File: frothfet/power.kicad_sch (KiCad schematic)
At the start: 46 parts, among them J11 Screw_Terminal_01x08, J12 Screw_Terminal_01x08, U26 TPS7A2033PDBVR, U27 XL1509-5.0, U28 MCP3425A0T-ECH, U29 MAX40200AUK

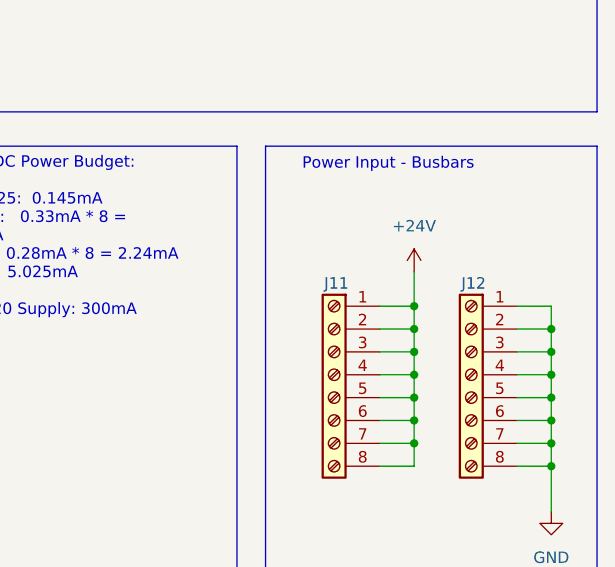
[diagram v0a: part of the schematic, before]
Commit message: rearranged leds and cleaned things up a bit.
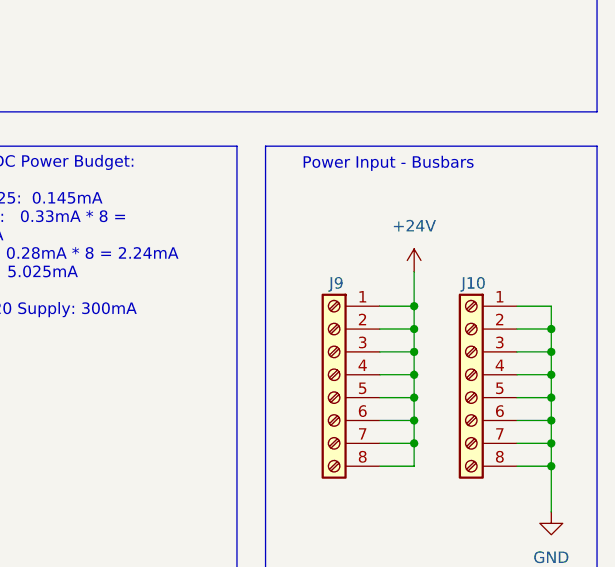
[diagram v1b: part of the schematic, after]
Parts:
- renumbered J12 to J10, J11 to J9
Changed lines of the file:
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@@
 		(on_board yes)
 		(dnp no)
-		(property "Reference" "J11"
+		(property "Reference" "J9"
 			(at 251.714 99.06 0)
 			(effects
@@
 			(project ""
 				(path "/c83c6236-96e9-46ad-9d7a-9e2efa4a7966/e112a34f-fd2f-43cb-bf5d-a7f5e57b6bef"
-					(reference "J11")
+					(reference "J9")
 					(unit 1)
 				)
@@
 		(dnp no)
 		(fields_autoplaced yes)
-		(property "Reference" "#PWR0135"
+		(property "Reference" "#PWR0131"
 			(at 19.05 102.87 0)
 			(effects
@@
 			(project "frothfet"
 				(path "/c83c6236-96e9-46ad-9d7a-9e2efa4a7966/e112a34f-fd2f-43cb-bf5d-a7f5e57b6bef"
-					(reference "#PWR0135")
+					(reference "#PWR0131")
 					(unit 1)
 				)
@@
 		(dnp no)
 		(fields_autoplaced yes)
-		(property "Reference" "#PWR0141"
+		(property "Reference" "#PWR0137"
 			(at 106.68 102.87 0)
 			(effects
@@
 			(project "frothfet"
 				(path "/c83c6236-96e9-46ad-9d7a-9e2efa4a7966/e112a34f-fd2f-43cb-bf5d-a7f5e57b6bef"
-					(reference "#PWR0141")
+					(reference "#PWR0137")
 					(unit 1)
 				)
@@
 		(dnp no)
 		(fields_autoplaced yes)
-		(property "Reference" "#PWR0137"
+		(property "Reference" "#PWR0133"
 			(at 30.48 161.29 0)
 			(effects
@@
 			(project "frothfet"
 				(path "/c83c6236-96e9-46ad-9d7a-9e2efa4a7966/e112a34f-fd2f-43cb-bf5d-a7f5e57b6bef"
-					(reference "#PWR0137")
+					(reference "#PWR0133")
 					(unit 1)
 				)
@@
 		(dnp no)
 		(fields_autoplaced yes)
-		(property "Reference" "#PWR0145"
+		(property "Reference" "#PWR0141"
 			(at 156.21 137.16 0)
 			(effects
@@
 			(project "frothfet"
 				(path "/c83c6236-96e9-46ad-9d7a-9e2efa4a7966/e112a34f-fd2f-43cb-bf5d-a7f5e57b6bef"
-					(reference "#PWR0145")
+					(reference "#PWR0141")
 					(unit 1)
 				)
@@
 		(dnp no)
 		(fields_autoplaced yes)
-		(property "Reference" "#PWR0140"
+		(property "Reference" "#PWR0136"
 			(at 86.36 100.33 0)
 			(effects
@@
 			(project ""
 				(path "/c83c6236-96e9-46ad-9d7a-9e2efa4a7966/e112a34f-fd2f-43cb-bf5d-a7f5e57b6bef"
-					(reference "#PWR0140")
+					(reference "#PWR0136")
 					(unit 1)
 				)
@@
 		(on_board yes)
 		(dnp no)
-		(property "Reference" "J12"
+		(property "Reference" "J10"
 			(at 266.954 99.06 0)
 			(effects
@@
 			(project ""
 				(path "/c83c6236-96e9-46ad-9d7a-9e2efa4a7966/e112a34f-fd2f-43cb-bf5d-a7f5e57b6bef"
-					(reference "J12")
+					(reference "J10")
 					(unit 1)
 				)
@@
 		(dnp no)
 		(fields_autoplaced yes)
-		(property "Reference" "#PWR0138"
+		(property "Reference" "#PWR0134"
 			(at 30.48 187.96 0)
 			(effects
@@
 			(project "frothfet"
 				(path "/c83c6236-96e9-46ad-9d7a-9e2efa4a7966/e112a34f-fd2f-43cb-bf5d-a7f5e57b6bef"
-					(reference "#PWR0138")
+					(reference "#PWR0134")
 					(unit 1)
 				)
@@
 		(dnp no)
 		(fields_autoplaced yes)
-		(property "Reference" "#PWR0142"
+		(property "Reference" "#PWR0138"
 			(at 138.43 107.95 0)
 			(effects
@@
 			(project "8ch-mosfet"
 				(path "/c83c6236-96e9-46ad-9d7a-9e2efa4a7966/e112a34f-fd2f-43cb-bf5d-a7f5e57b6bef"
-					(reference "#PWR0142")
+					(reference "#PWR0138")
 					(unit 1)
 				)
@@
 		(dnp no)
 		(fields_autoplaced yes)
-		(property "Reference" "#PWR0148"
+		(property "Reference" "#PWR0144"
 			(at 275.59 130.81 0)
 			(effects
@@
 			(project "8ch-mosfet"
 				(path "/c83c6236-96e9-46ad-9d7a-9e2efa4a7966/e112a34f-fd2f-43cb-bf5d-a7f5e57b6bef"
-					(reference "#PWR0148")
+					(reference "#PWR0144")
 					(unit 1)
 				)
@@
 		(dnp no)
 		(fields_autoplaced yes)
-		(property "Reference" "#PWR0146"
+		(property "Reference" "#PWR0142"
 			(at 260.35 101.6 0)
 			(effects
@@
 			(project "8ch-mosfet"
 				(path "/c83c6236-96e9-46ad-9d7a-9e2efa4a7966/e112a34f-fd2f-43cb-bf5d-a7f5e57b6bef"
-					(reference "#PWR0146")
+					(reference "#PWR0142")
 					(unit 1)
 				)
@@
 		(dnp no)
 		(fields_autoplaced yes)
-		(property "Reference" "#PWR0143"
+		(property "Reference" "#PWR0139"
 			(at 156.21 64.77 0)
 			(effects
@@
 			(project "8ch-mosfet"
 				(path "/c83c6236-96e9-46ad-9d7a-9e2efa4a7966/e112a34f-fd2f-43cb-bf5d-a7f5e57b6bef"
-					(reference "#PWR0143")
+					(reference "#PWR0139")
 					(unit 1)
 				)
@@
 		(dnp no)
 		(fields_autoplaced yes)
-		(property "Reference" "#PWR0147"
+		(property "Reference" "#PWR0143"
 			(at 266.7 33.02 0)
 			(effects
@@
 			(project "8ch-mosfet"
 				(path "/c83c6236-96e9-46ad-9d7a-9e2efa4a7966/e112a34f-fd2f-43cb-bf5d-a7f5e57b6bef"
-					(reference "#PWR0147")
+					(reference "#PWR0143")
 					(unit 1)
 				)
@@
 		(dnp no)
 		(fields_autoplaced yes)
-		(property "Reference" "#PWR0139"
+		(property "Reference" "#PWR0135"
 			(at 49.53 137.16 0)
 			(effects
@@
 			(project ""
 				(path "/c83c6236-96e9-46ad-9d7a-9e2efa4a7966/e112a34f-fd2f-43cb-bf5d-a7f5e57b6bef"
-					(reference "#PWR0139")
+					(reference "#PWR0135")
 					(unit 1)
 				)
@@
 		(dnp no)
 		(fields_autoplaced yes)
-		(property "Reference" "#PWR0136"
+		(property "Reference" "#PWR0132"
 			(at 22.86 33.02 0)
 			(effects
@@
 			(project "8ch-mosfet"
 				(path "/c83c6236-96e9-46ad-9d7a-9e2efa4a7966/e112a34f-fd2f-43cb-bf5d-a7f5e57b6bef"
-					(reference "#PWR0136")
+					(reference "#PWR0132")
 					(unit 1)
 				)
@@
 		(dnp no)
 		(fields_autoplaced yes)
-		(property "Reference" "#PWR0144"
+		(property "Reference" "#PWR0140"
 			(at 160.02 93.98 0)
 			(effects
@@
 			(project "frothfet"
 				(path "/c83c6236-96e9-46ad-9d7a-9e2efa4a7966/e112a34f-fd2f-43cb-bf5d-a7f5e57b6bef"
-					(reference "#PWR0144")
+					(reference "#PWR0140")
 					(unit 1)
 				)

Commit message: working on bom
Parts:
- renumbered F18 to F25, F19 to F26, J9 to J2, J10 to J3
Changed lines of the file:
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@@
 		(on_board yes)
 		(dnp no)
-		(property "Reference" "J9"
+		(property "Reference" "J2"
 			(at 251.714 99.06 0)
 			(effects
@@
 			(project ""
 				(path "/c83c6236-96e9-46ad-9d7a-9e2efa4a7966/e112a34f-fd2f-43cb-bf5d-a7f5e57b6bef"
-					(reference "J9")
+					(reference "J2")
 					(unit 1)
 				)
@@
 		(on_board yes)
 		(dnp no)
-		(property "Reference" "J10"
+		(property "Reference" "J3"
 			(at 266.954 99.06 0)
 			(effects
@@
 			(project ""
 				(path "/c83c6236-96e9-46ad-9d7a-9e2efa4a7966/e112a34f-fd2f-43cb-bf5d-a7f5e57b6bef"
-					(reference "J10")
+					(reference "J3")
 					(unit 1)
 				)
@@
 		(dnp no)
 		(fields_autoplaced yes)
-		(property "Reference" "F19"
+		(property "Reference" "F26"
 			(at 205.74 31.75 90)
 			(effects
@@
 			(project "8ch-mosfet"
 				(path "/c83c6236-96e9-46ad-9d7a-9e2efa4a7966/e112a34f-fd2f-43cb-bf5d-a7f5e57b6bef"
-					(reference "F19")
+					(reference "F26")
 					(unit 1)
 				)
@@
 		(dnp no)
 		(fields_autoplaced yes)
-		(property "Reference" "F18"
+		(property "Reference" "F25"
 			(at 34.29 31.75 90)
 			(effects
@@
 			(project "8ch-mosfet"
 				(path "/c83c6236-96e9-46ad-9d7a-9e2efa4a7966/e112a34f-fd2f-43cb-bf5d-a7f5e57b6bef"
-					(reference "F18")
-					(unit 1)
-				)
+					(reference "F25")
+					(unit 1)
+				)

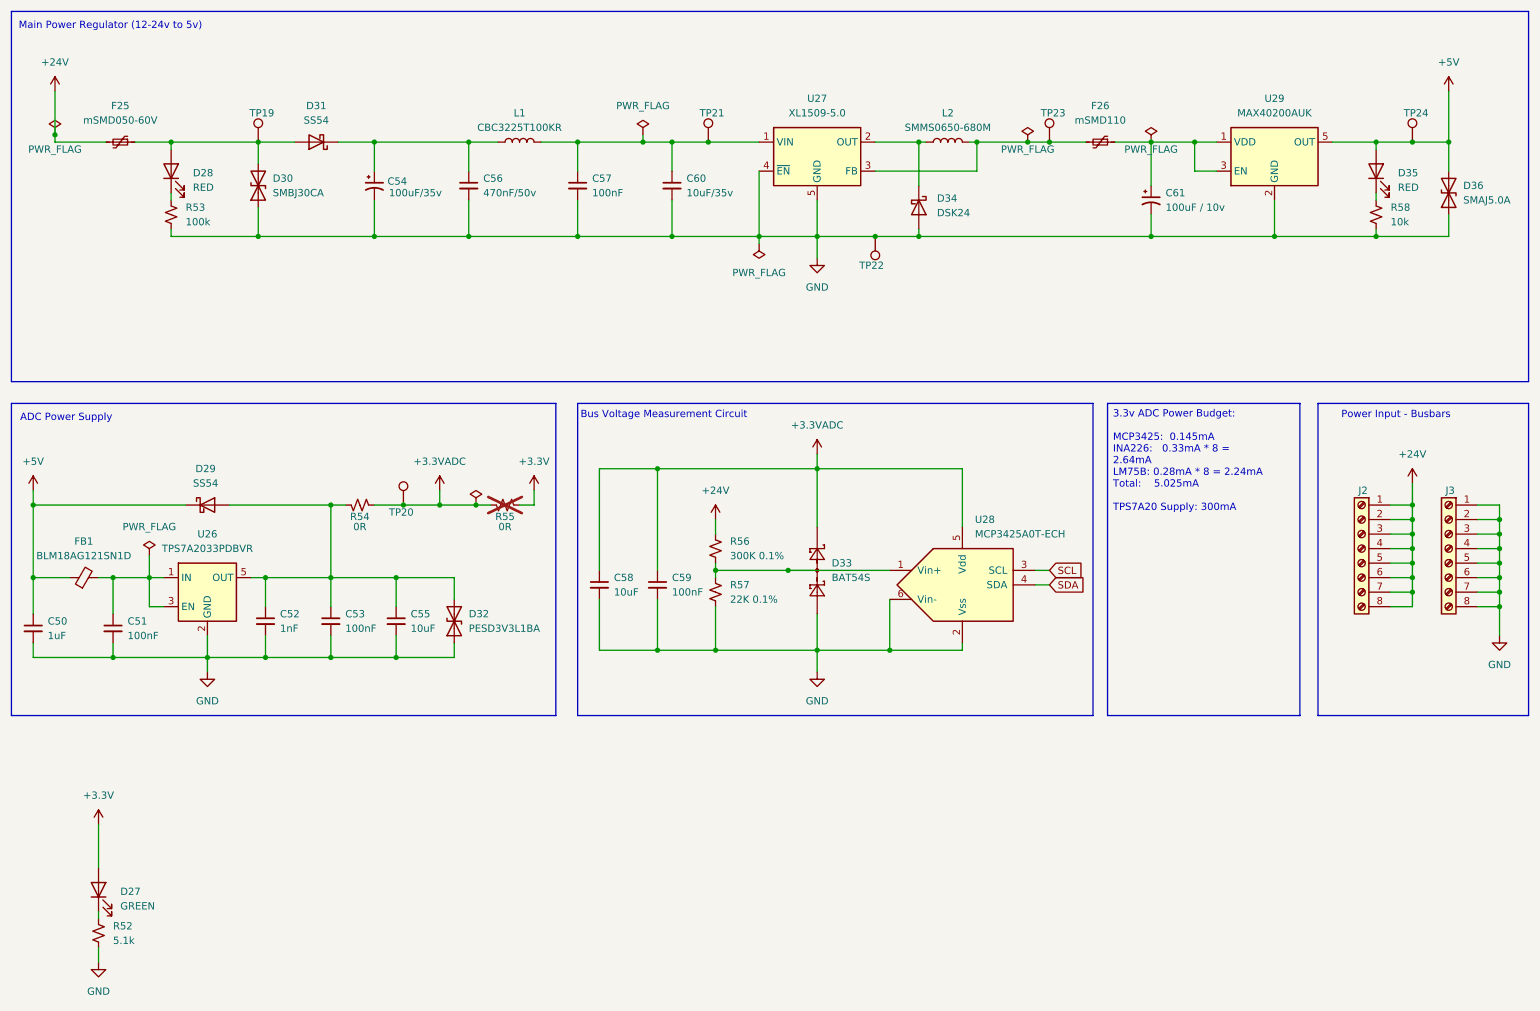
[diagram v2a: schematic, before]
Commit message: changed to XFCN 508 because 507 wasnt available on jlc
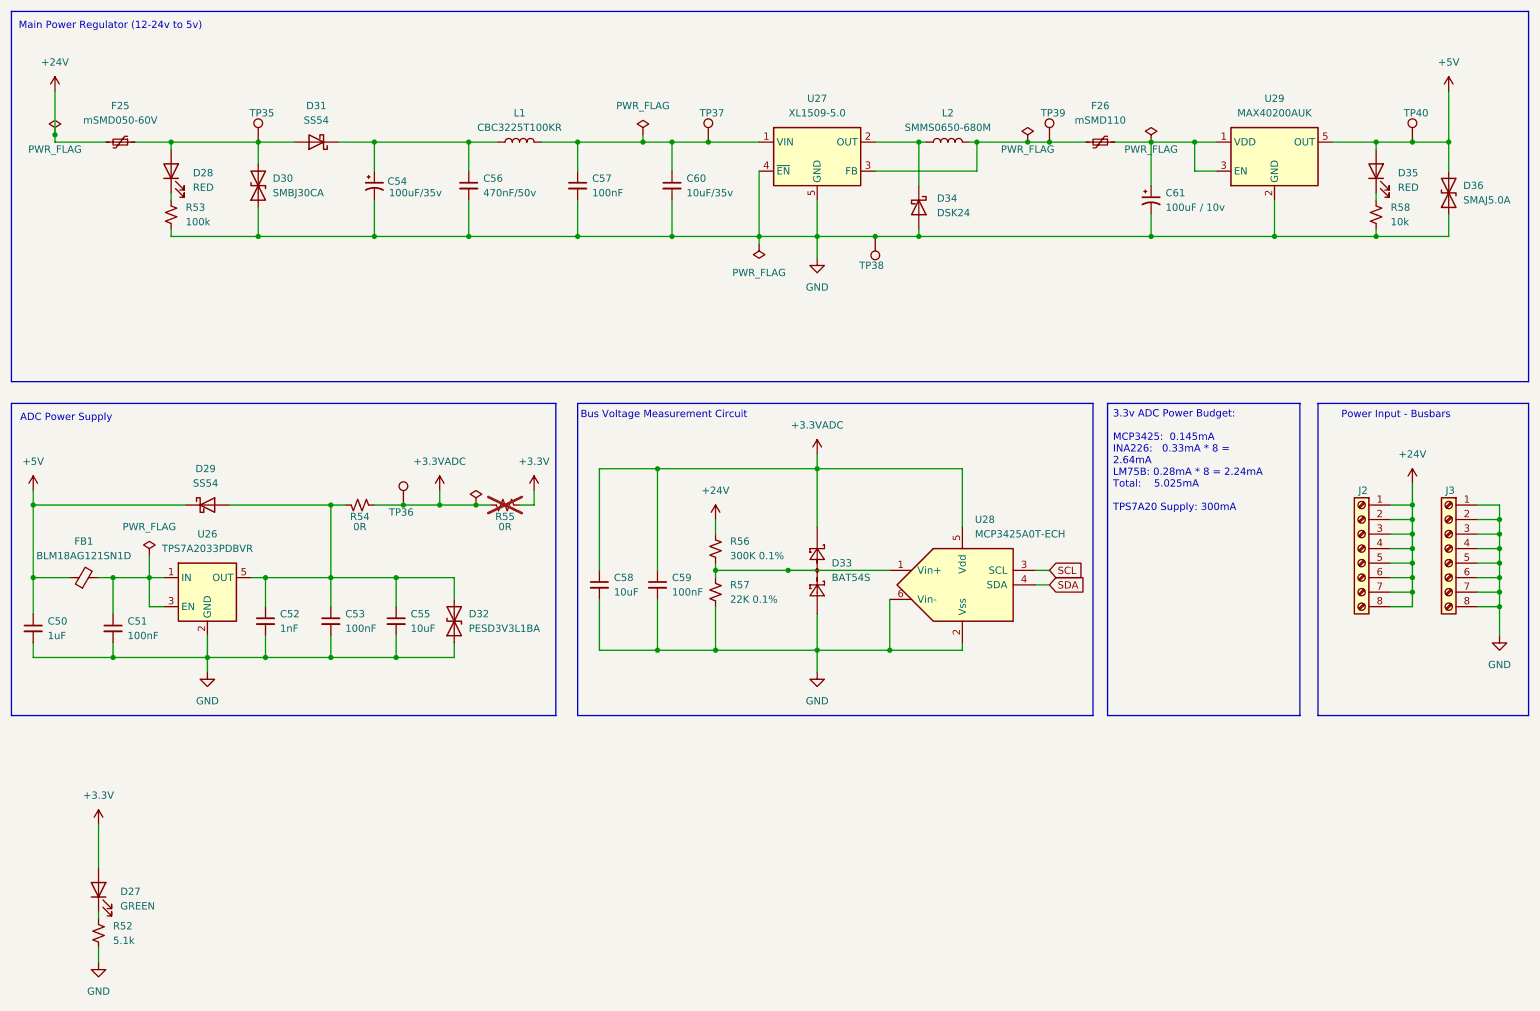
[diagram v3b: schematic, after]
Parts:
- renumbered TP19 to TP35, TP20 to TP36, TP21 to TP37, TP22 to TP38, TP23 to TP39, TP24 to TP40
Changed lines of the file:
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@@
 		(on_board yes)
 		(dnp no)
-		(property "Reference" "TP22"
+		(property "Reference" "TP38"
 			(at 167.894 59.69 0)
 			(effects
@@
 			(project "frothfet"
 				(path "/c83c6236-96e9-46ad-9d7a-9e2efa4a7966/e112a34f-fd2f-43cb-bf5d-a7f5e57b6bef"
-					(reference "TP22")
+					(reference "TP38")
 					(unit 1)
 				)
@@
 		(on_board yes)
 		(dnp no)
-		(property "Reference" "TP20"
+		(property "Reference" "TP36"
 			(at 81.28 102.87 0)
 			(effects
@@
 			(project ""
 				(path "/c83c6236-96e9-46ad-9d7a-9e2efa4a7966/e112a34f-fd2f-43cb-bf5d-a7f5e57b6bef"
-					(reference "TP20")
+					(reference "TP36")
 					(unit 1)
 				)
@@
 		(on_board yes)
 		(dnp no)
-		(property "Reference" "TP19"
+		(property "Reference" "TP35"
 			(at 56.896 33.02 0)
 			(effects
@@
 			(project "frothfet"
 				(path "/c83c6236-96e9-46ad-9d7a-9e2efa4a7966/e112a34f-fd2f-43cb-bf5d-a7f5e57b6bef"
-					(reference "TP19")
+					(reference "TP35")
 					(unit 1)
 				)
@@
 		(on_board yes)
 		(dnp no)
-		(property "Reference" "TP23"
+		(property "Reference" "TP39"
 			(at 195.326 33.02 0)
 			(effects
@@
 			(project "frothfet"
 				(path "/c83c6236-96e9-46ad-9d7a-9e2efa4a7966/e112a34f-fd2f-43cb-bf5d-a7f5e57b6bef"
-					(reference "TP23")
+					(reference "TP39")
 					(unit 1)
 				)
@@
 		(on_board yes)
 		(dnp no)
-		(property "Reference" "TP24"
+		(property "Reference" "TP40"
 			(at 258.826 33.02 0)
 			(effects
@@
 			(project "frothfet"
 				(path "/c83c6236-96e9-46ad-9d7a-9e2efa4a7966/e112a34f-fd2f-43cb-bf5d-a7f5e57b6bef"
-					(reference "TP24")
+					(reference "TP40")
 					(unit 1)
 				)
@@
 		(on_board yes)
 		(dnp no)
-		(property "Reference" "TP21"
+		(property "Reference" "TP37"
 			(at 135.636 33.02 0)
 			(effects
@@
 			(project "frothfet"
 				(path "/c83c6236-96e9-46ad-9d7a-9e2efa4a7966/e112a34f-fd2f-43cb-bf5d-a7f5e57b6bef"
-					(reference "TP21")
-					(unit 1)
-				)
+					(reference "TP37")
+					(unit 1)
+				)

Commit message: re-routed everything again
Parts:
- D28, D35: value RED -> GREEN; LCSC C2286 -> (none)
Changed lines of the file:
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@@
 			)
 		)
-		(property "Value" "RED"
+		(property "Value" "GREEN"
 			(at 46.99 46.0374 90)
 			(effects
@@
 			)
 		)
-		(property "LCSC" "C2286"
+		(property "LCSC" ""
 			(at 43.18 43.18 0)
 			(effects
@@
 			)
 		)
-		(property "Value" "RED"
+		(property "Value" "GREEN"
 			(at 257.81 46.0374 90)
 			(effects
@@
 			)
 		)
-		(property "LCSC" "C2286"
+		(property "LCSC" ""
 			(at 254 43.18 0)
 			(effects
